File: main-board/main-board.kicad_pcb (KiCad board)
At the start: 4 copper layers, 278.3 x 56.7 mm, 149 parts, among them J1 NCJ6FA-H-0, J10 SDS-50J, J11 Conn_02x14_Odd_Even, J12 Conn_02x02_Odd_Even, J13 Barrel_Jack_MountingPin, J14 Micro_SD_Card_Det2, J2 NCJ6FA-H-0, J3 Conn_02x10_Odd_Even, J4 NCJ6FA-H-0, J5 Conn_02x10_Odd_Even, J6 NCJ6FA-H-0, J7 SDS-50J, J8 Conn_02x03, J9 SDS-50J, Q1 MMBT3904, Q2 MMBT3906, Q3 MMBT3906, Q4 MMBT3904, Q5 DMP3056L-13, SW1 Power, U1 THAT1646, U10 TPS54302, U2 THAT1646, U3 OPA1656ID, U4 THAT1246, U5 THAT1246, U6 OPA1656ID, U7 LM2903, U8 H11L1, U9 Daisy_Seed

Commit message: wip: working on splitting the daughter board
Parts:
- removed D10, D9: LED, LED_THT:LED_D3.0mm
- removed H3: MountingHole, MountingHole:MountingHole_3.2mm_M3
- removed J5: Conn_02x10_Odd_Even, Connector_IDC:IDC-Header_2x10_P2.54mm_Vertical
- removed RV1, RV3, RV5, RV6: 10k log, Potentiometer_THT:Potentiometer_Alpha_RD901F-40-00D_Single_Vertical_CircularHoles
- moved C38 46.7 mm to (240.9, 49.5)
- moved C42 46.7 mm to (234.8, 64.4)
- moved H11 46.7 mm to (251.8, 77.5)
- moved L1 46.7 mm to (251.6, 51.7)
- moved Q5 46.7 mm to (232.2, 36.4)
- moved R33 46.7 mm to (234.4, 32.4)
- moved R36 46.7 mm to (242.1, 55.7)
- moved C1 46.7 mm to (41.8, 62.9)
- moved C10 46.7 mm to (76.3, 70.5)
- moved C12 46.7 mm to (103.9, 59.9)
- moved C16 46.7 mm to (88.2, 64.8)
- moved C19 46.7 mm to (125.0, 59.9)
- moved C2 46.7 mm to (37.0, 69.1)
- moved C21 46.7 mm to (121.6, 59.9)
- moved C22 46.7 mm to (110.1, 65.4)
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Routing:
- net CLIP_LED_K_R: track 145.7 -> 79.8 mm
- net CLIP_LED_A_R: track 66.7 -> 6.78 mm
- net CLIP_LED_A_L: track 59.6 -> 14.3 mm
- net CLIP_LED_K_L: track 109.9 -> 68.9 mm
- net IN_OPA_R: track 53.4 -> 27.5 mm
- net OUT_OPA_L: track 51.9 -> 26.4 mm
- net OUT_WIPER_L: track 87.9 -> 62.4 mm
- net IN_WIPER_R: track 57.4 -> 35.1 mm
- net OUT_OPA_R: track 44.6 -> 30.9 mm
- net OUT_WIPER_R: track 54.5 -> 40.8 mm
- net IN_OPA_L: track 28.9 -> 22.4 mm
- net IN_WIPER_L: track 40.4 -> 33.9 mm
- net GND: vias 2186 -> 1779
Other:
- board size 278.3 x 56.7 mm -> 241.7 x 56.7 mm
- board text removed: "Gain/Clip Daisy-Studio Rev2b 29 Apr 2026 Rasheed Abdul-Aziz"
- board text removed: "V-Groove"

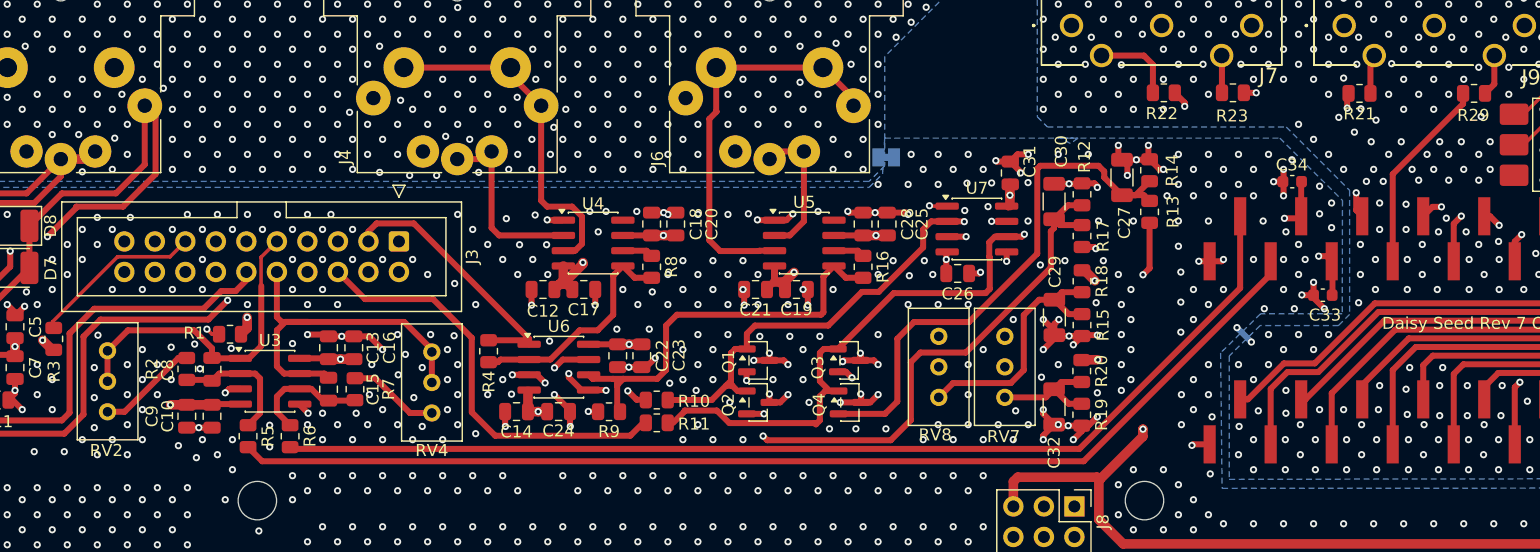
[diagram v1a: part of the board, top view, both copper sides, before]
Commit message: swap and label rv8/7 so they lay out clearly
fixes #21
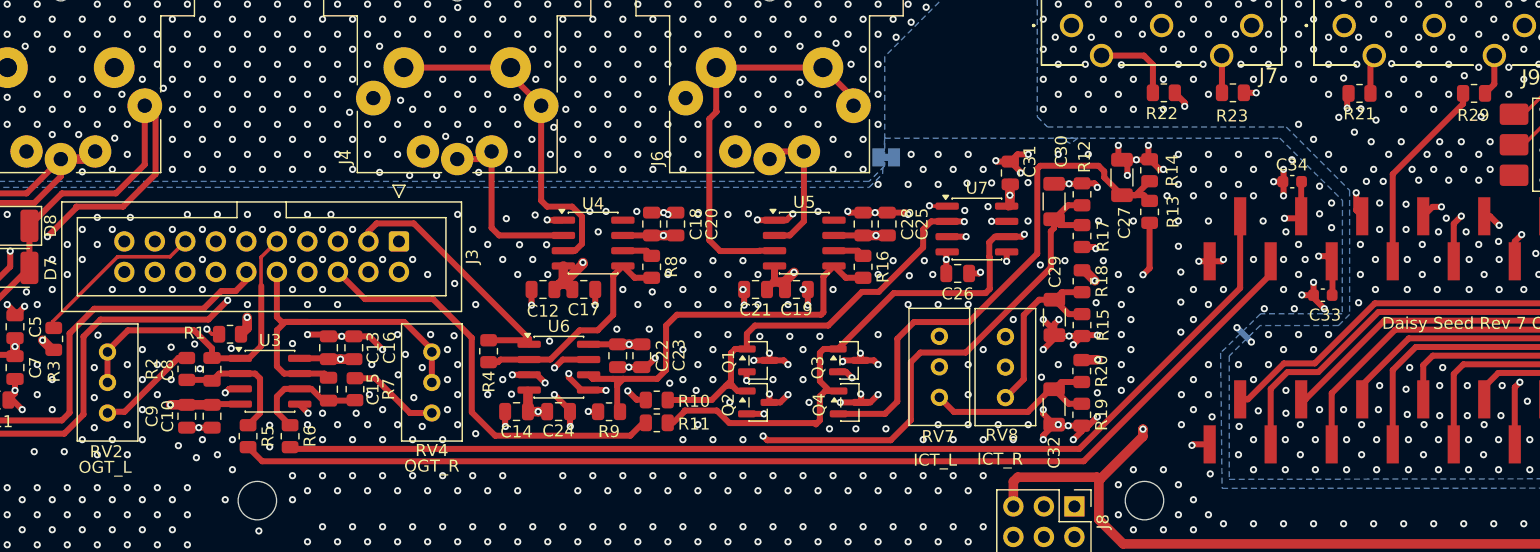
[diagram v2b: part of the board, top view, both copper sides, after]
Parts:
- moved RV8 5.55 mm to (142.4, 68.9)
- moved RV7 5.45 mm to (136.9, 68.9)
- moved RV2 0.10 mm to (67.7, 65.1)
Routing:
- net /Audio Input/IN_THRESH_L: track 17.5 -> 15.0 mm
- net +VCLAMP_L: track 31.8 -> 33.4 mm
- net /Audio Input/IN_THRESH_R: track 11.9 -> 10.7 mm
- net GND: vias 1779 -> 1778
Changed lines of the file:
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@@
 			)
 		)
+		(property "Label" "OGT_R"
+			(at -9.5 0 0)
+			(unlocked yes)
+			(layer "F.SilkS")
+			(effects
+				(font
+					(size 1 1)
+					(thickness 0.15)
+				)
+			)
+		)
 		(property ki_fp_filters "Potentiometer*")
 		(sheetname "/Audio Output/")
@@
 	(footprint "Potentiometer_THT:Potentiometer_Bourns_3296W_Vertical"
 		(layer "F.Cu")
-		(at 67.65 65 90)
+		(at 67.65 65.1 90)
 		(descr "Potentiometer, vertical, Bourns 3296W, https://www.bourns.com/pdfs/3296.pdf")
 		(tags "Potentiometer vertical Bourns 3296W")
@@
 			)
 		)
+		(property "Label" "OGT_L"
+			(at -9.6 -0.2 0)
+			(unlocked yes)
+			(layer "F.SilkS")
+			(effects
+				(font
+					(size 1 1)
+					(thickness 0.15)
+				)
+			)
+		)
 		(property ki_fp_filters "Potentiometer*")
 		(sheetname "/Audio Output/")
@@
 	(footprint "Potentiometer_THT:Potentiometer_Bourns_3296W_Vertical"
 		(layer "F.Cu")
-		(at 136.85 68.88 -90)
+		(at 142.4 68.9 -90)
 		(descr "Potentiometer, vertical, Bourns 3296W, https://www.bourns.com/pdfs/3296.pdf")
 		(tags "Potentiometer vertical Bourns 3296W")
 		(property "Reference" "RV8"
-			(at 3.12 0.3 180)
+			(at 3.12 0.3 0)
 			(layer "F.SilkS")
 			(effects
@@
 			)
 		)
+		(property "Label" "ICT_R"
+			(at 5.12 0.45 0)
+			(unlocked yes)
+			(layer "F.SilkS")
+			(effects
+				(font
+					(size 1 1)
+					(thickness 0.15)
+				)
+			)
+		)
 		(property ki_fp_filters "Potentiometer*")
 		(sheetname "/Audio Input/")
@@
 	(footprint "Potentiometer_THT:Potentiometer_Bourns_3296W_Vertical"
 		(layer "F.Cu")
-		(at 142.35 68.88 -90)
+		(at 136.9 68.88 -90)
 		(descr "Potentiometer, vertical, Bourns 3296W, https://www.bourns.com/pdfs/3296.pdf")
 		(tags "Potentiometer vertical Bourns 3296W")
 		(property "Reference" "RV7"
-			(at 3.26 0.105 180)
+			(at 3.26 0.105 0)
 			(layer "F.SilkS")
 			(effects
@@
 			)
 		)
+		(property "Label" "ICT_L"
+			(at 5.22 0.35 0)
+			(unlocked yes)
+			(layer "F.SilkS")
+			(effects
+				(font
+					(size 1 1)
+					(thickness 0.15)
+				)
+			)
+		)
 		(property ki_fp_filters "Potentiometer*")
 		(sheetname "/Audio Input/")
@@
 	)
 	(via
-		(at 143.25 70)
-		(size 0.6)
-		(drill 0.3)
-		(layers "F.Cu" "B.Cu")
-		(free yes)
-		(net 1)
-	)
-	(via
 		(at 23.05 72.4)
 		(size 0.6)
@@
 	)
 	(via
-		(at 180.55 42.4)
+		(at 180.6 42.1)
 		(size 0.6)
 		(drill 0.3)
@@
 	(segment
 		(start 143.925 62.025)
-		(end 143.925 66.607329)
-		(width 0.5)
-		(layer "F.Cu")
-		(net 24)
-	)
-	(segment
-		(start 143.925 66.607329)
-		(end 142.843329 67.689)
-		(width 0.5)
-		(layer "F.Cu")
-		(net 24)
-	)
-	(segment
-		(start 142.843329 67.689)
-		(end 138.041 67.689)
+		(end 143.925 67.375)
 		(width 0.5)
 		(layer "F.Cu")
@@
 	)
 	(segment
-		(start 138.041 67.689)
-		(end 136.85 68.88)
+		(start 143.925 67.375)
+		(end 142.4 68.9)
 		(width 0.5)
 		(layer "F.Cu")
@@
 	(segment
 		(start 129.625 67.25)
-		(end 135.22 67.25)
+		(end 129.975 67.6)
 		(width 0.5)
 		(layer "In1.Cu")
@@
 	)
 	(segment
-		(start 135.22 67.25)
-		(end 136.85 68.88)
+		(start 141.1 67.6)
+		(end 142.4 68.9)
+		(width 0.5)
+		(layer "In1.Cu")
+		(net 24)
+	)
+	(segment
+		(start 129.975 67.6)
+		(end 141.1 67.6)
 		(width 0.5)
 		(layer "In1.Cu")
@@
 	)
 	(segment
-		(start 145.77 68.88)
-		(end 146.45 68.2)
+		(start 136.9 68.88)
+		(end 138.111 70.091)
 		(width 0.5)
 		(layer "F.Cu")
@@
 	)
 	(segment
-		(start 142.35 68.88)
-		(end 145.77 68.88)
+		(start 144.268641 70.091)
+		(end 146.159641 68.2)
+		(width 0.5)
+		(layer "F.Cu")
+		(net 26)
+	)
+	(segment
+		(start 138.111 70.091)
+		(end 144.268641 70.091)
+		(width 0.5)
+		(layer "F.Cu")
+		(net 26)
+	)
+	(segment
+		(start 146.159641 68.2)
+		(end 146.45 68.2)
 		(width 0.5)
 		(layer "F.Cu")
@@
 	(segment
 		(start 122.3 70.25)
-		(end 140.98 70.25)
+		(end 133.9 70.25)
+		(width 0.5)
+		(layer "In1.Cu")
+		(net 26)
+	)
+	(segment
+		(start 134.2 70.25)
+		(end 134.5 70.25)
 		(width 0.5)
 		(layer "In1.Cu")
@@
 	)
 	(segment
-		(start 140.98 70.25)
-		(end 142.35 68.88)
+		(start 135.53 70.25)
+		(end 136.9 68.88)
+		(width 0.5)
+		(layer "In1.Cu")
+		(net 26)
+	)
+	(segment
+		(start 133.9 70.25)
+		(end 135.53 70.25)
+		(width 0.5)
+		(layer "In1.Cu")
+		(net 26)
+	)
+	(segment
+		(start 133.9 70.25)
+		(end 134.2 70.25)
 		(width 0.5)
 		(layer "In1.Cu")
@@
 	)
 	(segment
-		(start 143.775 56.1)
-		(end 144.05 56.375)
+		(start 141.096 57.471)
+		(end 141.096 62.144)
 		(width 0.5)
 		(layer "In1.Cu")
@@
 	)
 	(segment
-		(start 144.05 56.375)
-		(end 144.05 64.64)
-		(width 0.5)
-		(layer "In1.Cu")
-		(net 79)
-	)
-	(segment
-		(start 139.725 56.1)
-		(end 143.775 56.1)
+		(start 141.096 62.144)
+		(end 136.9 66.34)
 		(width 0.5)
 		(layer "In1.Cu")
@@
 	(segment
 		(start 139.125 55.5)
-		(end 139.725 56.1)
-		(width 0.5)
-		(layer "In1.Cu")
-		(net 79)
-	)
-	(segment
-		(start 144.05 64.64)
-		(end 142.35 66.34)
+		(end 141.096 57.471)
 		(width 0.5)
 		(layer "In1.Cu")
@@
 	)
 	(segment
-		(start 142.5 60.69)
-		(end 136.85 66.34)
+		(start 143.821 58.871)
+		(end 143.821 64.939)
+		(width 0.5)
+		(layer "In1.Cu")
+		(net 80)
+	)
+	(segment
+		(start 143.821 64.939)
+		(end 142.4 66.36)
 		(width 0.5)
 		(layer "In1.Cu")
@@
 	(segment
 		(start 142.5 57.55)
-		(end 142.5 60.69)
+		(end 143.821 58.871)
 		(width 0.5)
 		(layer "In1.Cu")

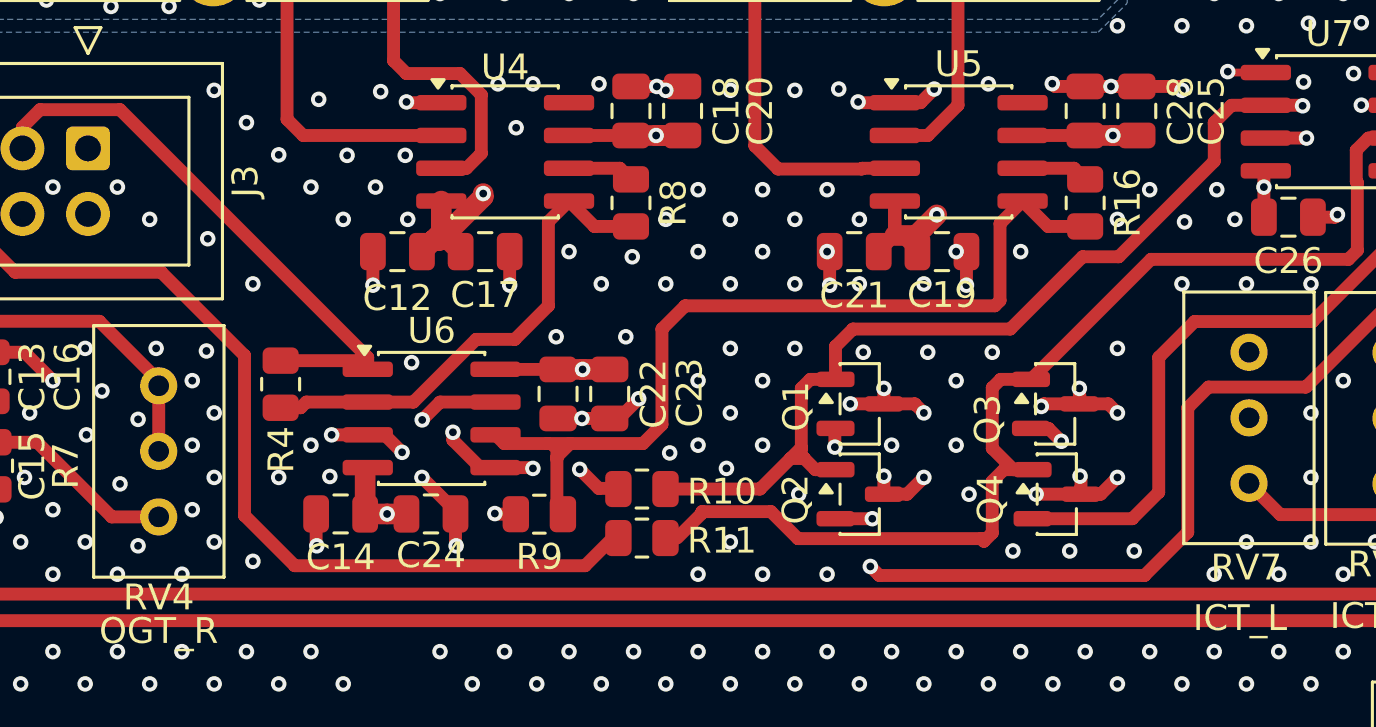
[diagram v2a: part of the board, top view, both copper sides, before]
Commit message: fix sense error for output topology
fixes #20
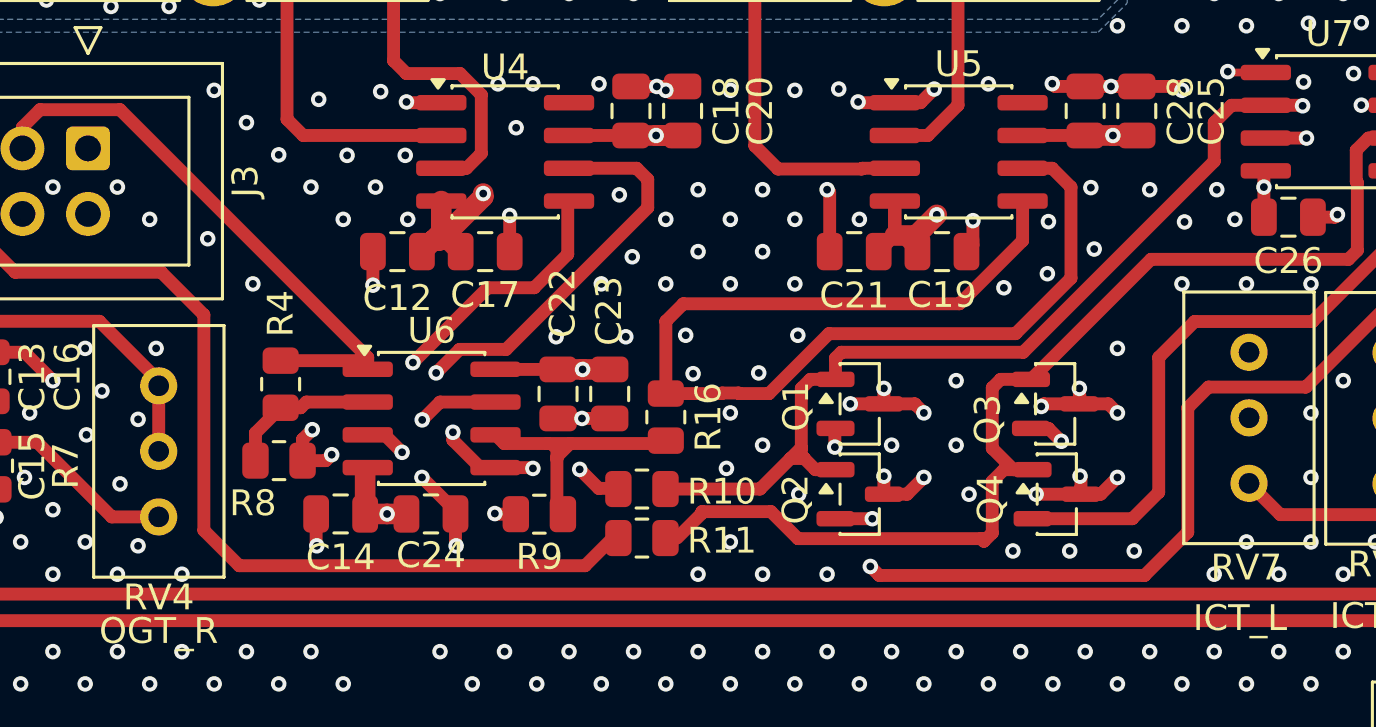
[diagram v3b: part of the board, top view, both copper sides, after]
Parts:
- moved R16 18.2 mm to (114.3, 66.3)
- moved R8 16.9 mm to (99.3, 68.0), turned to 180 degrees
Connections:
- R16 pad 1: Net-(R16-Pad1) -> Net-(U5A-S)
- R16 pad 2: Net-(U5A-S) -> Net-(U6B--)
- R4 pad 1: Net-(U4A-S) -> Net-(U6A--)
- R8 pad 1: Net-(R8-Pad1) -> Net-(U4A-S)
- R8 pad 2: Net-(U4A-S) -> Net-(U6A--)
- R9 pad 1: Net-(U5A-S) -> Net-(U6B--)
- U4 pad 6: Net-(R8-Pad1) -> Net-(U4A-S)
- U5 pad 6: Net-(R16-Pad1) -> Net-(U5A-S)
- U6 pad 2: Net-(U4A-S) -> Net-(U6A--)
- U6 pad 6: Net-(U5A-S) -> Net-(U6B--)
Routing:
- net Net-(U4A-S): track 19.2 -> 37.9 mm, vias 0 -> 4
- net Net-(U6B--): track 0.00 -> 10.3 mm
- net Net-(U5A-S): track 34.7 -> 42.7 mm
- net Net-(U6A--): track 0.00 -> 5.92 mm
- net Net-(R16-Pad1): track 2.60 -> 0.00 mm
- net Net-(R8-Pad1): track 2.58 -> 0.00 mm
- net IN_WIPER_R: track 35.1 -> 36.4 mm
- net GND: track 240.2 -> 239.0 mm, vias 1778 -> 1757

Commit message: make threshold trimmer 100k so it doesn't drag down the clamp ref +ve rail
fixes #19
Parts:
- RV7, RV8: value 10k -> 100k
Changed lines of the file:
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@@
 			)
 		)
-		(property "Value" "10k"
+		(property "Value" "100k"
 			(at -2.54 3.67 90)
 			(layer "F.Fab")
@@
 			)
 		)
-		(property "Value" "10k"
+		(property "Value" "100k"
 			(at -2.54 3.67 90)
 			(layer "F.Fab")

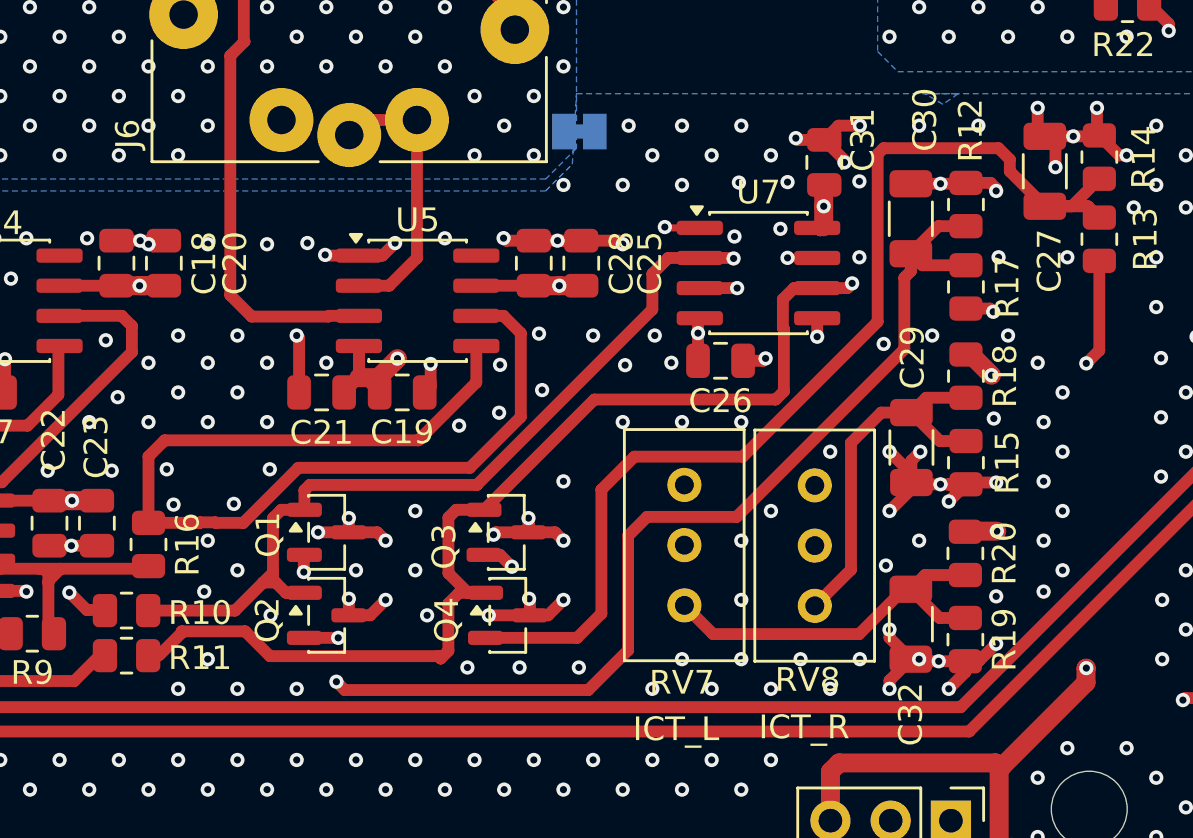
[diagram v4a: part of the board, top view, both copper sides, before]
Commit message: fix footprint on the clamp transistors
fixes #18
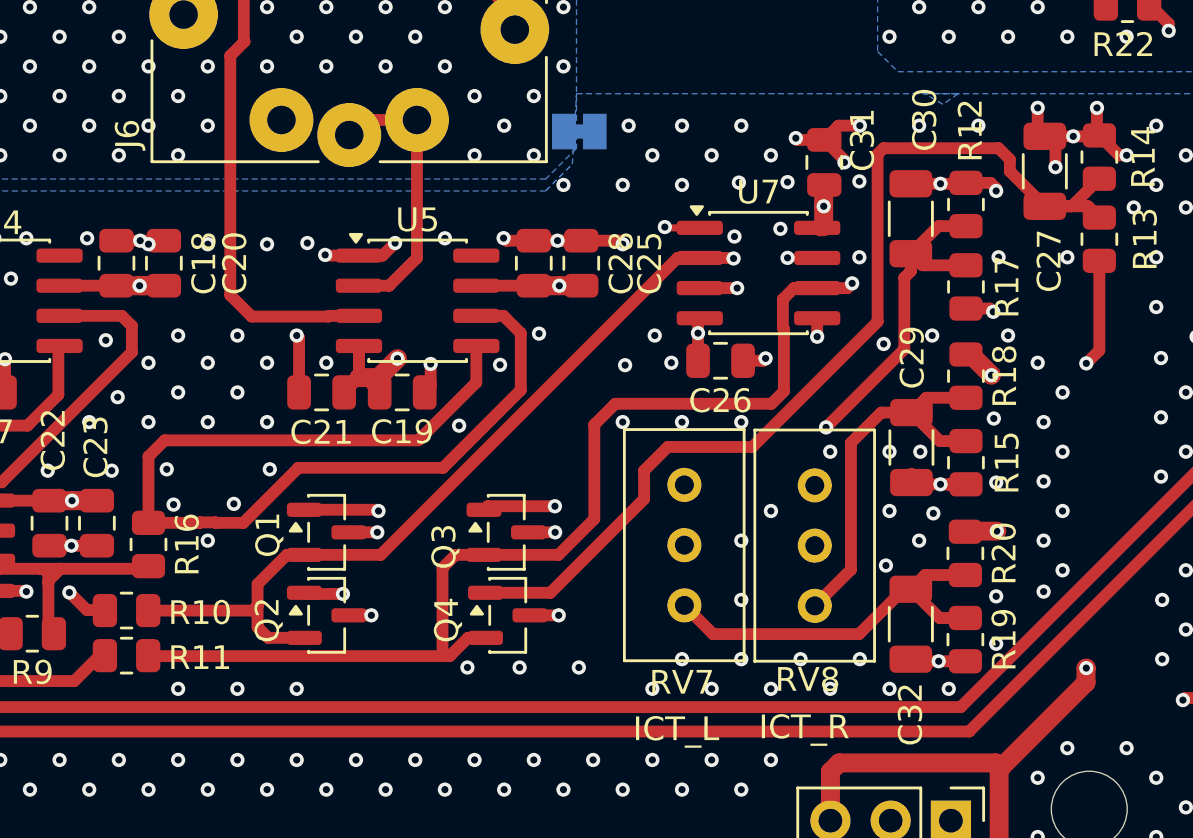
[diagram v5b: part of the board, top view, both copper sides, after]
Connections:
- Q1 pad 1: AUDIO_IN_L -> -VCLAMP_L
- Q1 pad 2: -VCLAMP_L -> AUDIO_IN_L
- Q2 pad 1: AUDIO_IN_L -> +VCLAMP_L
- Q2 pad 2: +VCLAMP_L -> AUDIO_IN_L
- Q3 pad 1: AUDIO_IN_R -> +VCLAMP_R
- Q3 pad 2: +VCLAMP_R -> AUDIO_IN_R
- Q4 pad 1: AUDIO_IN_R -> -VCLAMP_R
- Q4 pad 2: -VCLAMP_R -> AUDIO_IN_R
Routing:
- net GND: track 239.0 -> 216.8 mm, vias 1757 -> 1736
- net -VCLAMP_L: track 48.2 -> 38.5 mm
- net -VCLAMP_R: track 45.9 -> 42.8 mm
- net AUDIO_IN_L: track 73.0 -> 71.9 mm
- net +VCLAMP_L: track 33.4 -> 32.4 mm
- net +VCLAMP_R: track 30.8 -> 31.7 mm
- net Net-(U5A-S): track 42.7 -> 42.1 mm
